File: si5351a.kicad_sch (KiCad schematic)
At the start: 11 parts, among them J8 CLK2, U4 MS5351M

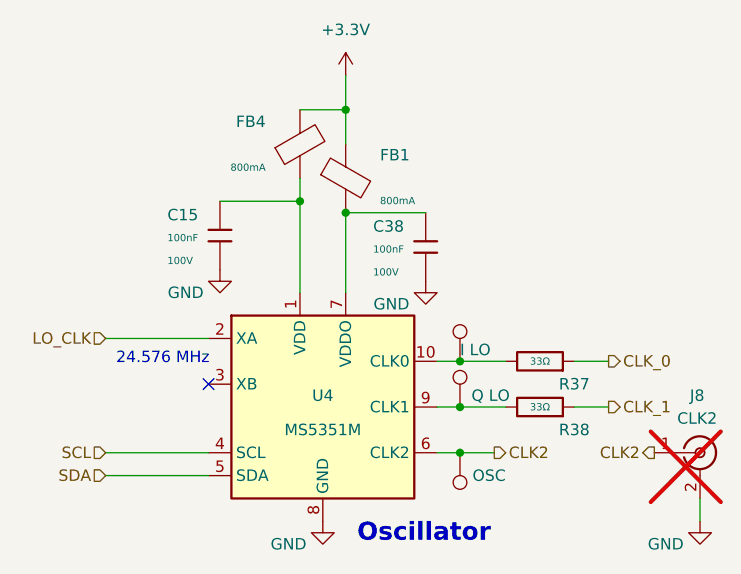
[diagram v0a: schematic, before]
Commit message: Editing 6 layer
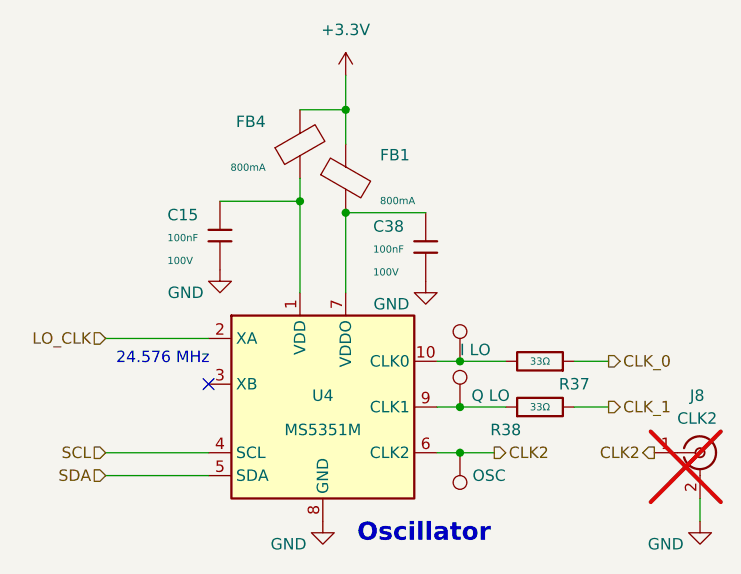
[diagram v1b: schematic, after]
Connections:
- net CLK_1: now also R38.2; no longer R38.1
- net at TP4.1, U4.9 (CLK1): now also R38.1; no longer R38.2
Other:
- moved on the sheet: R38
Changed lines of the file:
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@@
 	(symbol
 		(lib_id "PCM_JLCPCB-Resistors:0805,33Ω")
-		(at 163.83 113.03 270)
-		(mirror x)
+		(at 163.83 113.03 90)
 		(unit 1)
 		(exclude_from_sim no)
@@
 		(dnp no)
 		(property "Reference" "R38"
-			(at 167.64 115.57 90)
+			(at 160.02 115.57 90)
 			(effects
 				(font
